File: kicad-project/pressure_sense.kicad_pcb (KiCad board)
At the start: 2 copper layers, 71.5 x 86.2 mm, 30 parts

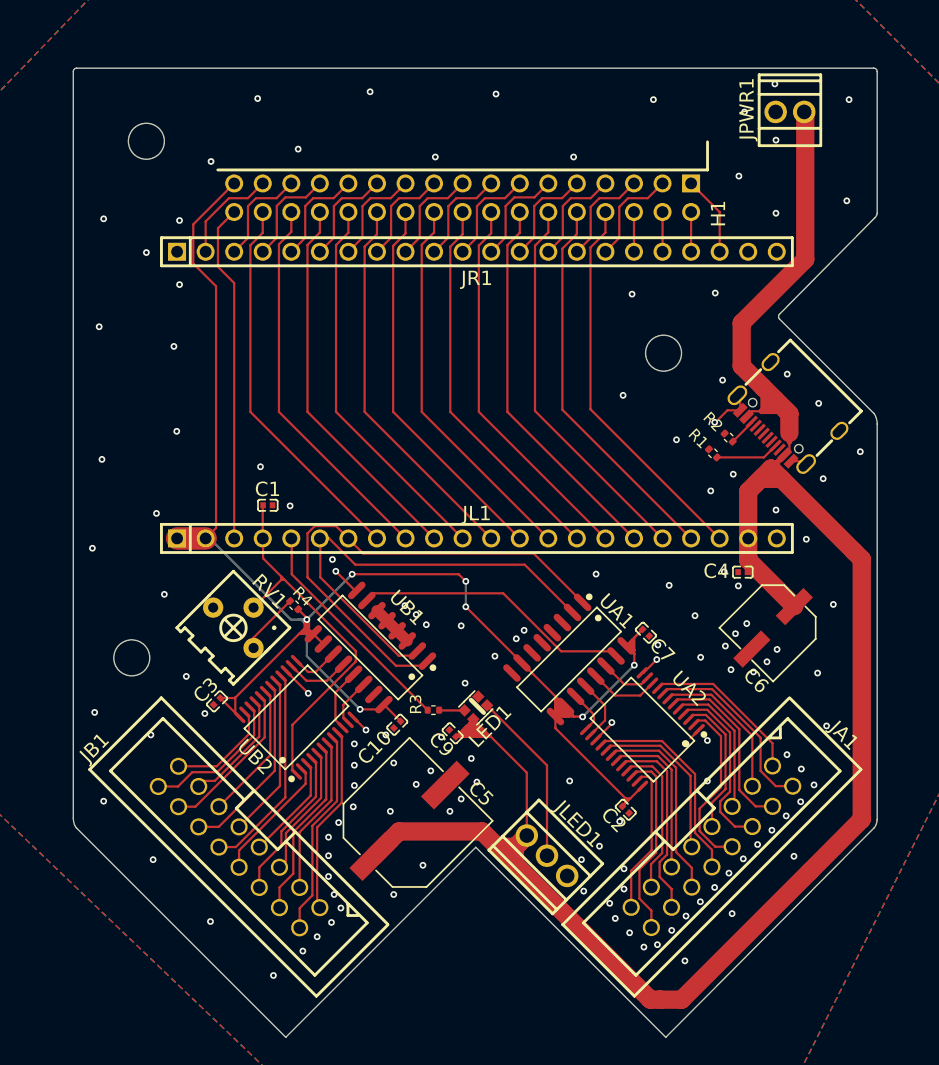
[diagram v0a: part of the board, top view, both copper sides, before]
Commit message: cleaning up footprints
used easyeda2kicad.py to get better footprints (with 3d models) (https://github.com/uPesy/easyeda2kicad.py)

it's kinda messy bc some symbols are kicad and others easyeda, shouldn't matter tho (e.g. on C6 can't see the 470u value, only part ref)
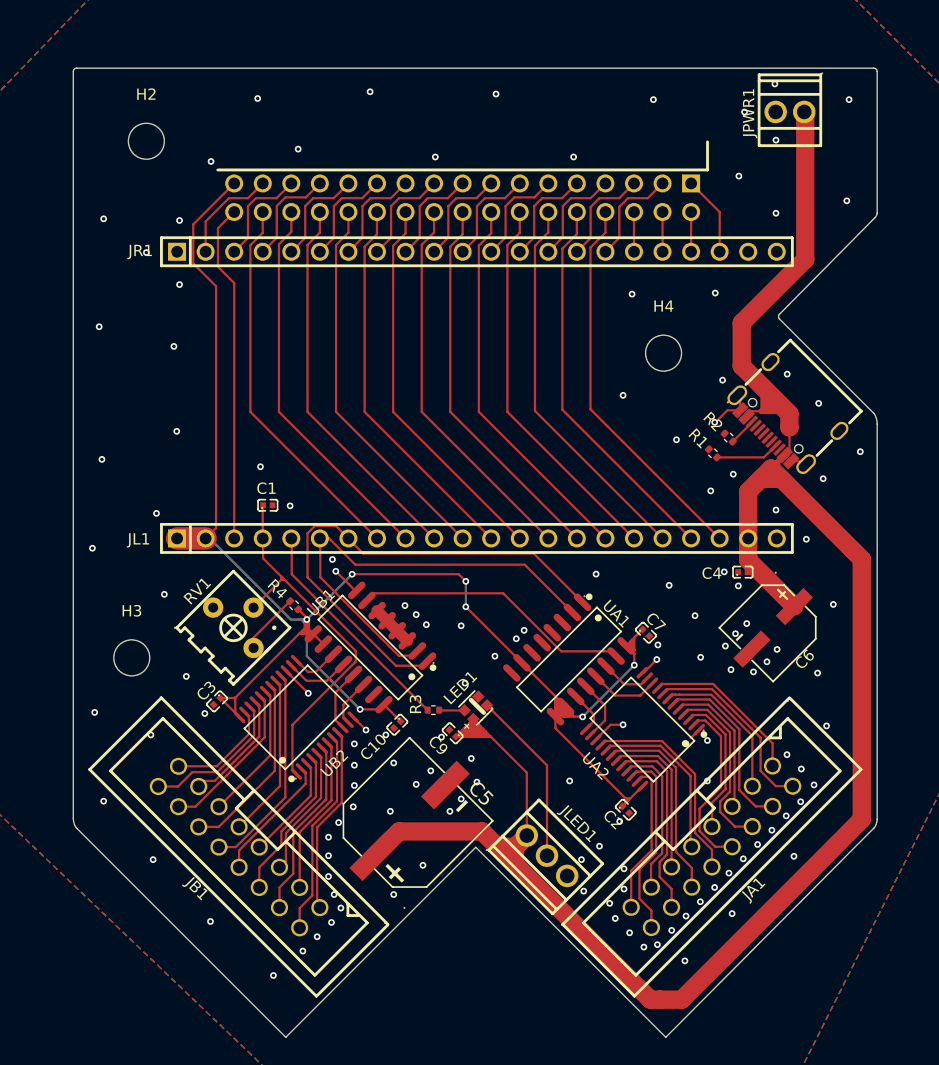
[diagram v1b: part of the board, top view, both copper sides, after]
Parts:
- removed H1: X6521WR-2×17H-C30D60, 2*17P:HDR-TH_34P-P2.54-H-M-R2-C17-S2.54
- removed REF** (x3): MountingHole_3.2mm_M3, MountingHole:MountingHole_3.2mm_M3
- added H2: MountingHole, MountingHole:MountingHole_3.2mm_M3, F.Cu at (68.8, 21.9)
- added H3: MountingHole, MountingHole:MountingHole_3.2mm_M3, F.Cu at (67.5, 67.8)
- added H4: MountingHole, MountingHole:MountingHole_3.2mm_M3, F.Cu at (114.8, 40.8)
- added H5: X6521WR-2×17H-C30D60, easyeda2kicad:HDR-TH_34P-P2.54-H-M-R2-C17-S2.54, F.Cu at (96.9, 26.9)
- C1, C10, C2, C3, C4, C7, C9: footprint 100nF:C0402 -> easyeda2kicad:C0402
- C5: footprint 1000uF:CAP-SMD_BD10.0-L10.3-W10.3-LS11.3-FD -> easyeda2kicad:CAP-SMD_BD10.0-L10.3-W10.3-FD
- C6: value 470u -> UT1A471M0607VG; footprint 470uF:CAP-SMD_BD6.3-L6.6-W6.6-FD -> easyeda2kicad:CAP-SMD_BD6.3-L6.6-W6.6-FD
- JA1, JB1: footprint IDC:IDC-TH_16P-P2.54_C3406 -> easyeda2kicad:IDC-TH_16P-P2.54_C3406
- JL1, JR1: value Conn_01x22_Socket -> FH2.54-09-22PZD; footprint 22P:HDR-TH_22P-P2.54-V-M -> easyeda2kicad:HDR-TH_22P-P2.54-V-M
- JLED1: footprint 3P:CONN-TH_3P-P2.54_KF128-2.54-3P -> easyeda2kicad:CONN-TH_3P-P2.54_KF128-2.54-3P
- JPWR1: value Screw_Terminal_01x02 -> KF128-2.54-2P; footprint 2P:CONN-TH_P2.54_KF128-2.54-2P -> easyeda2kicad:CONN-TH_P2.54_KF128-2.54-2P
- LED1: footprint _WS2812B-2020-V6:LED-SMD_4P-L2.2-W2.0-P1.00_WS2815C-2020-4P -> easyeda2kicad:LED-SMD_4P-L2.2-W2.0-P1.00_WS2815C-2020-4P
- RV1: value 20k -> 3362P-1-203_C118933; footprint pot:RES-ADJ-TH_3P-L7.1-W6.9-P2.50-L_3362P -> easyeda2kicad:RES-ADJ-TH_3P-L7.1-W6.9-P2.50-L_3362P
- UA1, UB1: footprint SN74HC163DR:SOIC-16_L9.9-W3.9-P1.27-LS6.0-BL -> easyeda2kicad:SOIC-16_L9.9-W3.9-P1.27-LS6.0-BL
- UA2, UB2: footprint CD74HC4067SM96:SSOP-24_L8.1-W5.3-P0.65-LS7.8-BL -> easyeda2kicad:SSOP-24_L8.1-W5.3-P0.65-LS7.8-BL
- USBC1: footprint USBC:USB-C_SMD-TYPE-C-31-M-12_1 -> easyeda2kicad:USB-C_SMD-TYPE-C-31-M-12_1
- turned C4 to 0 degrees
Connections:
- C4 pad 1: +5V -> GND
- C4 pad 2: GND -> +5V
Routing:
- net GND: track 21.8 -> 22.7 mm

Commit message: changed capacitor for cost
the two smd caps cost extra $6 just for the toolhead! I changed it to one tht that is hand-soldered (the leads need to be bent)
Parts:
- removed C6: UT1A471M0607VG, easyeda2kicad:CAP-SMD_BD6.3-L6.6-W6.6-FD
- C5: footprint easyeda2kicad:CAP-SMD_BD10.0-L10.3-W10.3-FD -> footprints:cap_flat
- moved C5 36.0 mm to (124.4, 66.3), turned to 90 degrees
- moved JLED1 12.6 mm to (91.8, 85.4), turned to 45 degrees
- moved C9 11.9 mm to (96.5, 62.7), turned to 45 degrees
- moved C7 7.62 mm to (107.3, 70.3), turned to 135 degrees
- moved UA2 7.53 mm to (107.6, 79.5)
- moved UA1 7.53 mm to (101.0, 73.3)
- moved C2 7.42 mm to (106.1, 86.6)
- moved LED1 7.25 mm to (98.1, 65.1)
- moved C4 5.92 mm to (121.9, 54.3)
- moved R3 5.50 mm to (96.4, 67.4), turned to 90 degrees
- moved C10 0.84 mm to (91.7, 73.2), turned to 45 degrees
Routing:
- net +3.3V: track 164.1 -> 134.3 mm, vias 7 -> 5
- net GND: track 22.7 -> 32.2 mm, vias 137 -> 134
- net /Dout: track 15.6 -> 24.3 mm
- net /I7A: track 15.8 -> 11.3 mm
- net /I8A: track 13.6 -> 9.54 mm
- net /I9A: track 17.0 -> 13.1 mm
- net /I10A: track 13.9 -> 10.5 mm
- net /I6A: track 12.8 -> 9.46 mm
- net /I11A: track 17.4 -> 14.0 mm
- net /I5A: track 15.9 -> 13.7 mm
- net /I0A: track 14.6 -> 16.7 mm
- net /D5: track 20.3 -> 22.2 mm
- net /I12A: track 14.2 -> 12.3 mm
- net /D6: track 40.4 -> 41.9 mm
- net /I1A: track 17.0 -> 18.4 mm
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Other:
- board text removed: "C5"

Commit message: production files processed, and keep out zone added
going through the jlcpcb order process, adjusting cpl (positions) and checking the price

JLCPCB Fabrication Toolkit doesn't listen to my selection of "exclude from pick and place file" for mounting holes, so I had to delete them manually
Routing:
- net +3.3V: track 134.3 -> 136.4 mm
- net GND: track 32.2 -> 34.2 mm, vias 134 -> 122
- net /D7: track 46.5 -> 47.1 mm

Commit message: changed usbc port
the port had tiny pads, i changed it for a less dodgy 6p one cause I don't need data

dw I adjusted positions.csv
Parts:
- removed USBC1: TYPE-C-31-M-12, easyeda2kicad:USB-C_SMD-TYPE-C-31-M-12_1
- added USB1: TYPE-C 6P, easyeda2kicad:TYPE-C-SMD_TYPE-C-6P_1, F.Cu at (125.6, 46.3)
- moved R1 3.88 mm to (123.0, 50.4), turned to -135 degrees
- moved H4 1.59 mm to (113.4, 40.0)
- moved R2 1.24 mm to (121.6, 49.0), turned to 45 degrees
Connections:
- JR1 pad 1: GND -> unconnected-(JR1-Pad1)
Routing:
- net Net-(USB1-CC1): track 5.64 -> 2.41 mm
- net GND: track 34.2 -> 31.4 mm
- net +5V: track 192.7 -> 194.4 mm, vias 0 -> 4

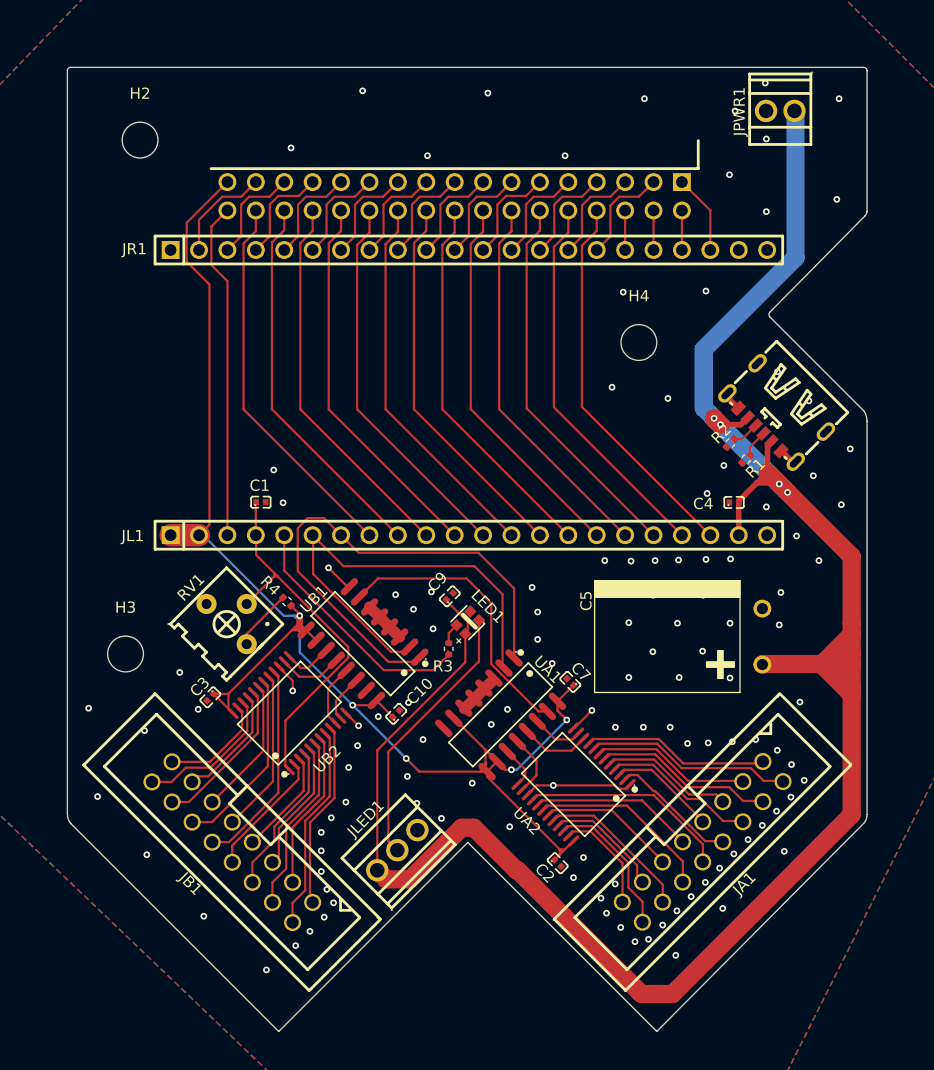
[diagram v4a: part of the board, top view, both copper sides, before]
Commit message: BIG CHANGE TO PCB
So since there's actually more time on Fallout, I decided to make the schematic simpler (so it's cheaper and smaller) by removing the uneccesary 74hc163 counters (there's plenty of gpio!)
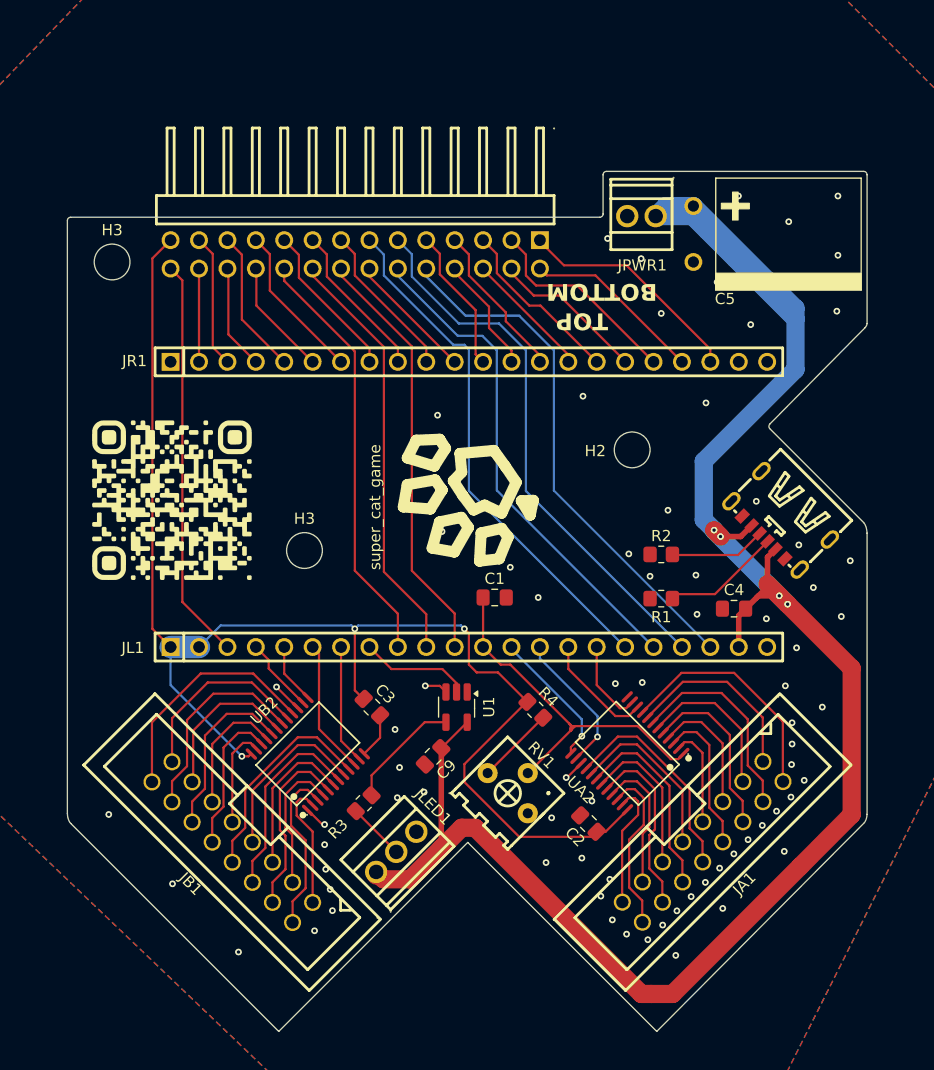
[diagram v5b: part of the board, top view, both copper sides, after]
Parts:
- removed C10, C7: 100n, easyeda2kicad:C0402
- removed H4: MountingHole, MountingHole:MountingHole_3.2mm_M3
- removed H5: X6521WR-2×17H-C30D60, easyeda2kicad:HDR-TH_34P-P2.54-H-M-R2-C17-S2.54
- removed LED1: WS2812B-2020-V6, easyeda2kicad:LED-SMD_4P-L2.2-W2.0-P1.00_WS2815C-2020-4P
- removed UA1, UB1: SN74HC163DR_C338758, easyeda2kicad:SOIC-16_L9.9-W3.9-P1.27-LS6.0-BL
- added G***: LOGO, qr:qr_small, F.Cu at (71.7, 54.1)
- added H3: MountingHole, MountingHole:MountingHole_3.2mm_M3, F.Cu at (66.3, 32.8)
- added J1: Conn_02x14_Odd_Even, easyeda2kicad:HDR-TH_28P-P2.54-H-M-R2-C14-S2.54, F.Cu at (88.0, 32.1)
- added U1: SN74LV1T34DBV, Package_TO_SOT_SMD:SOT-23-5_HandSoldering, F.Cu at (97.1, 72.6)
- C1, C2, C3, C4, C9: footprint easyeda2kicad:C0402 -> Capacitor_SMD:C_0805_2012Metric_Pad1.18x1.45mm_HandSolder
- R1, R2, R3, R4: footprint Resistor_SMD:R_0402_1005Metric -> Resistor_SMD:R_0805_2012Metric_Pad1.20x1.40mm_HandSolder
- moved H2 52.0 mm to (112.8, 49.6)
- moved C5 36.5 mm to (118.3, 30.3), turned to -90 degrees
- moved RV1 29.3 mm to (102.6, 79.4)
- moved R4 24.2 mm to (104.1, 72.8), turned to -45 degrees
- moved C1 22.6 mm to (100.5, 62.8)
- moved H3 18.5 mm to (83.5, 58.6)
- moved R3 15.8 mm to (88.8, 81.2), turned to -135 degrees
- moved JPWR1 15.6 mm to (113.6, 28.7)
- moved R1 14.6 mm to (115.4, 62.9), turned to 180 degrees
- moved C3 14.5 mm to (89.5, 72.6), turned to -45 degrees
- moved C9 14.4 mm to (95.0, 77.0), turned to -135 degrees
- moved R2 11.7 mm to (115.4, 58.9), turned to 0 degrees
- moved JR1 10.0 mm to (98.2, 41.7)
- moved JL1 10.0 mm to (98.2, 67.2)
- moved USB1 9.65 mm to (126.0, 56.0)
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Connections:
- C1 pad 1: /D4 -> /D8
- JA1 pad 1: /I0A -> /I1A
- JA1 pad 2: /I1A -> /I0A
- JA1 pad 3: /I2A -> /I3A
- JA1 pad 4: /I3A -> /I2A
- JA1 pad 5: /I4A -> /I5A
- JA1 pad 6: /I5A -> /I4A
- JA1 pad 7: /I6A -> /I7A
- JA1 pad 8: /I7A -> /I6A
- JB1 pad 1: /I0B -> /I7B
- JB1 pad 10: /I15B -> /I9B
- JB1 pad 11: /I12B -> /I10B
- JB1 pad 12: /I13B -> /I11B
- JB1 pad 13: /I10B -> /I12B
- JB1 pad 14: /I11B -> /I13B
- JB1 pad 15: /I8B -> /I14B
- JB1 pad 16: /I9B -> /I15B
- JB1 pad 2: /I1B -> /I6B
- JB1 pad 3: /I2B -> /I5B
- JB1 pad 4: /I3B -> /I4B
- JB1 pad 5: /I4B -> /I3B
- JB1 pad 6: /I5B -> /I2B
- JB1 pad 7: /I6B -> /I1B
- JB1 pad 8: /I7B -> /I0B
- JB1 pad 9: /I14B -> /I8B
- R3 pad 1: /D5 -> Net-(U1-Y)
- R3 pad 2: Net-(LED1-DI) -> /Dout
- RV1 pad 1: unconnected-(RV1-Pad1) -> Net-(R4-Pad2)
- RV1 pad 2: /D4 -> /D8
- RV1 pad 3: Net-(R4-Pad2) -> unconnected-(RV1-Pad3)
- UA2 pad 1: GND -> /D8
- UA2 pad 10: /QB1 -> /D9
- UA2 pad 11: /QA1 -> /D10
- UA2 pad 13: /QD1 -> /D3
- UA2 pad 14: /QC1 -> /D46
- UB2 pad 1: /D4 -> GND
- UB2 pad 10: /QB2 -> /D6
- UB2 pad 11: /QA2 -> /D7
- UB2 pad 13: /QD2 -> /D5
- UB2 pad 14: /QC2 -> /D4
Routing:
- net /D7: track 47.1 -> 10.7 mm
- net /D6: track 42.3 -> 12.0 mm
- net /D4: track 34.2 -> 6.71 mm
- net /D10: track 34.2 -> 7.67 mm
- net /RCO: track 25.6 -> 0.00 mm
- net /D15: track 34.2 -> 9.91 mm
- net /D9: track 34.2 -> 10.2 mm
- net /D3: track 34.2 -> 12.5 mm, vias 0 -> 1
- net /D46: track 34.2 -> 12.9 mm, vias 0 -> 1
- net /Dout: track 24.3 -> 5.15 mm
- net GND: track 31.4 -> 12.7 mm, vias 122 -> 74
- net +5V: track 194.4 -> 177.0 mm
- net /D5: track 22.2 -> 5.44 mm
- net /D21: track 3.54 -> 18.3 mm
- net /D13: track 34.3 -> 49.0 mm
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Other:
- board size 71.5 x 86.2 mm -> 71.5 x 76.9 mm
- board text added: "By Ayden Yak For FALLOUT"
- board text added: "Melbourne, AUS, 2026!"
- board text added: "super_cat_game"

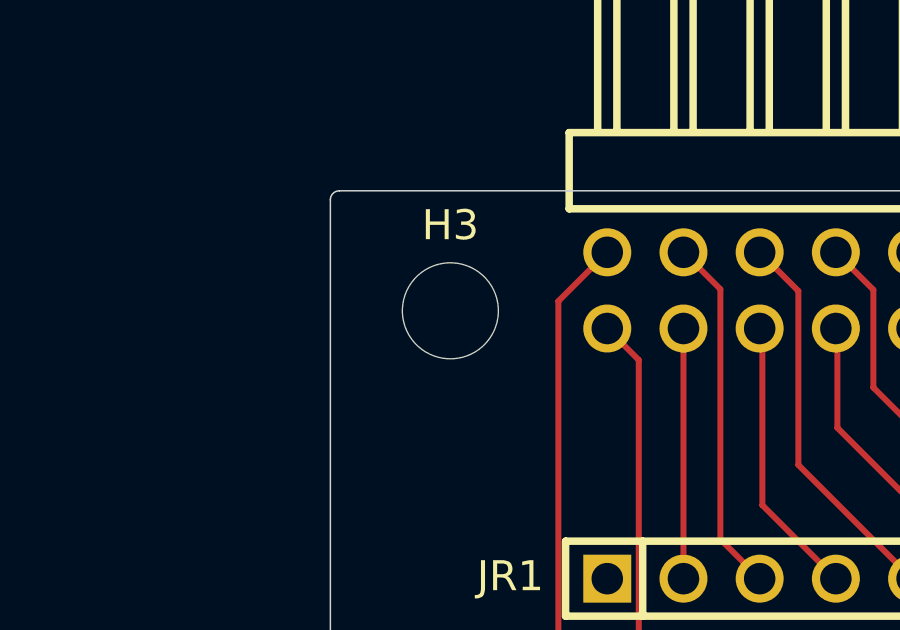
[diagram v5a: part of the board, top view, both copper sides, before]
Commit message: Oops, fixing the production files
I forgot to update the production files, and since I'm not going to do PCBA anymore, I deleted the pick-and-place file... the BOM should now be correct tho!
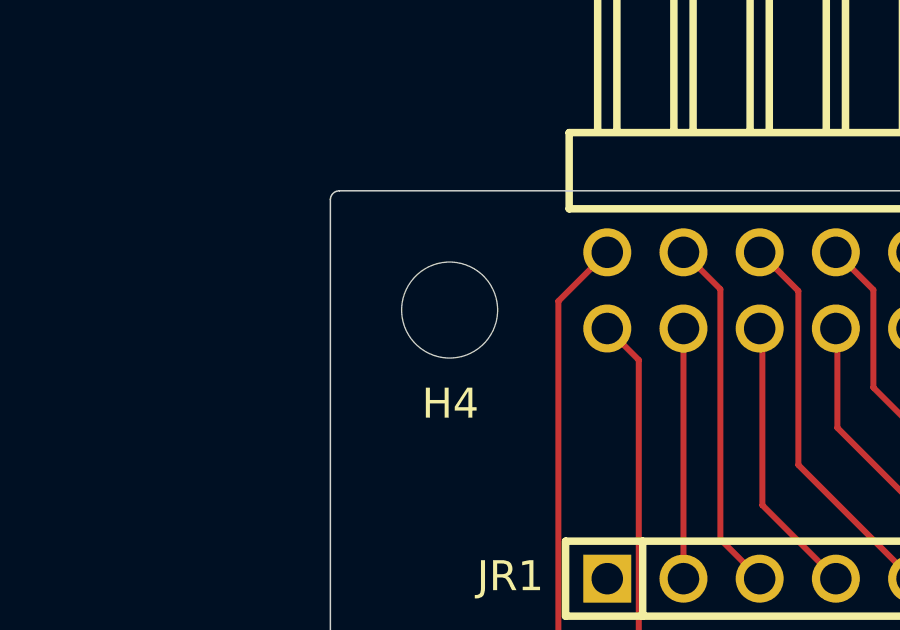
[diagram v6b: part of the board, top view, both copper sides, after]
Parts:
- removed the H3 at (66.3, 32.8)
- added H4: MountingHole, MountingHole:MountingHole_3.2mm_M3, F.Cu at (66.3, 32.8)
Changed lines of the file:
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@@
 		(sheetname "/")
 		(sheetfile "pressure_sense.kicad_sch")
+		(units
+			(unit
+				(name "A")
+				(pins "1" "3" "5" "7" "9" "11" "13" "15" "17" "19" "21" "23" "25" "27"
+					"2" "4" "6" "8" "10" "12" "14" "16" "18" "20" "22" "24" "26" "28"
+				)
+			)
+		)
 		(attr through_hole)
 		(duplicate_pad_numbers_are_jumpers no)
@@
 	(footprint "MountingHole:MountingHole_3.2mm_M3"
 		(layer "F.Cu")
-		(at 83.5 58.6)
+		(at 66.275 32.775)
 		(descr "Mounting Hole 3.2mm, M3, no annular, generated by kicad-footprint-generator mountinghole.py")
 		(tags "mountinghole M3")
-		(property "Reference" "H3"
-			(at 0 -2.85 0)
+		(property "Reference" "H4"
+			(at 0.025 3.125 0)
 			(layer "F.SilkS")
 			(effects
@@
 	(footprint "MountingHole:MountingHole_3.2mm_M3"
 		(layer "F.Cu")
-		(at 66.3 32.8)
+		(at 83.5 58.6)
 		(descr "Mounting Hole 3.2mm, M3, no annular, generated by kicad-footprint-generator mountinghole.py")
 		(tags "mountinghole M3")
@@
 		(sheetname "/")
 		(sheetfile "pressure_sense.kicad_sch")
+		(units
+			(unit
+				(name "A")
+				(pins)
+			)
+		)
 		(attr exclude_from_pos_files exclude_from_bom)
 		(duplicate_pad_numbers_are_jumpers no)
